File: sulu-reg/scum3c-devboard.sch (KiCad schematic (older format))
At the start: 36 parts, among them J1 Conn_02x11_Odd_Even, J2 Conn_02x10_Odd_Even, J3 Conn_02x05_Odd_Even, J4 73391-0060, U2 S-85S1AB18-I6T1U, U3 S-85S1AB11-I6T1U, U9AB1 ICM-20948

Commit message: finished routing
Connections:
- net +1.1V_REG: now also J1.8 (Pin_8); no longer J1.10 (Pin_10)
- net +1.8V_REG: now also J1.4 (Pin_4), J1.6 (Pin_6); no longer J1.14 (Pin_14), J1.16 (Pin_16)
- net +EXT_BAT: now also J1.12 (Pin_12), J1.9 (Pin_9); no longer J1.11 (Pin_11), J1.18 (Pin_18)
- net +VBAT: now also J1.17 (Pin_17), J1.5 (Pin_5); no longer J1.13 (Pin_13), J1.7 (Pin_7)
- net +VDDD: now also J1.7 (Pin_7); no longer J1.9 (Pin_9)
- net +VDDIO: now also J1.13 (Pin_13), J1.15 (Pin_15), J1.18 (Pin_18); no longer J1.3 (Pin_3), J1.5 (Pin_5), J1.8 (Pin_8)
- net 1.1V_IN: now also J1.10 (Pin_10); no longer J1.12 (Pin_12)
- net GND: now also J1.11 (Pin_11), J1.3 (Pin_3); no longer J1.15 (Pin_15), J1.17 (Pin_17)
- net IMU_VDD: now also J1.16 (Pin_16); no longer J1.6 (Pin_6)
- net IMU_VDDIO: now also J1.14 (Pin_14); no longer J1.4 (Pin_4)
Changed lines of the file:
@@
 Text Label 1700 1750 2    50   ~ 0
 IMU_VDDIO
-Text Label 1800 6900 0    50   ~ 0
+Text Label 1800 7400 0    50   ~ 0
 IMU_VDDIO
 Text Label 3800 7300 0    50   ~ 0
@@
 Text Label 3800 7600 0    50   ~ 0
 GPIO15
-Text Label 1800 7000 0    50   ~ 0
+Text Label 1800 7500 0    50   ~ 0
 IMU_VDD
 NoConn ~ 1300 2950
@@
 	0    1    1    0
 $EndComp
-Text Label 1800 7700 0    50   ~ 0
-BOOT_SOURCE_SEL
 Text Label 5450 7150 0    50   ~ 0
 3WB_DATA
@@
 	0    1    1    0
 $EndComp
-Text Label 1300 7800 2    50   ~ 0
-SENSOR_EXT_IN
-Text Label 1800 7800 0    50   ~ 0
-SENSOR_LDO_OUTPUT
 Text Label 4950 6950 2    50   ~ 0
 RsRx
@@
 L draft1library:+VDDIO #PWR?
 U 1 1 6076CC41
-P 1300 7000
+P 1300 7500
 AR Path="/5F3B1D81/6076CC41" Ref="#PWR?"  Part="1"
 AR Path="/6076CC41" Ref="#PWR05"  Part="1"
-F 0 "#PWR05" H 1300 6850 50  0001 C CNN
-F 1 "+VDDIO" V 1315 7128 50  0000 L CNN
-F 2 "" H 1300 7000 50  0001 C CNN
-F 3 "" H 1300 7000 50  0001 C CNN
-	1    1300 7000
+F 0 "#PWR05" H 1300 7350 50  0001 C CNN
+F 1 "+VDDIO" V 1315 7628 50  0000 L CNN
+F 2 "" H 1300 7500 50  0001 C CNN
+F 3 "" H 1300 7500 50  0001 C CNN
+	1    1300 7500
 	0    -1   -1   0
 $EndComp
@@
 L draft1library:+VDDIO #PWR?
 U 1 1 6076D2AC
-P 1300 6900
+P 1300 7400
 AR Path="/5F3B1D81/6076D2AC" Ref="#PWR?"  Part="1"
 AR Path="/6076D2AC" Ref="#PWR04"  Part="1"
-F 0 "#PWR04" H 1300 6750 50  0001 C CNN
-F 1 "+VDDIO" V 1315 7028 50  0000 L CNN
-F 2 "" H 1300 6900 50  0001 C CNN
-F 3 "" H 1300 6900 50  0001 C CNN
-	1    1300 6900
+F 0 "#PWR04" H 1300 7250 50  0001 C CNN
+F 1 "+VDDIO" V 1315 7528 50  0000 L CNN
+F 2 "" H 1300 7400 50  0001 C CNN
+F 3 "" H 1300 7400 50  0001 C CNN
+	1    1300 7400
 	0    -1   -1   0
 $EndComp
@@
 L draft1library:+VBAT #PWR?
 U 1 1 6076D7B9
-P 1300 7100
+P 1300 7600
 AR Path="/5F3B1D81/6076D7B9" Ref="#PWR?"  Part="1"
 AR Path="/5F41418C/6076D7B9" Ref="#PWR?"  Part="1"
 AR Path="/5F414989/6076D7B9" Ref="#PWR?"  Part="1"
 AR Path="/6076D7B9" Ref="#PWR06"  Part="1"
-F 0 "#PWR06" H 1300 6950 50  0001 C CNN
-F 1 "+VBAT" V 1300 7400 50  0000 C CNN
-F 2 "" H 1300 7100 50  0001 C CNN
-F 3 "" H 1300 7100 50  0001 C CNN
-	1    1300 7100
+F 0 "#PWR06" H 1300 7450 50  0001 C CNN
+F 1 "+VBAT" V 1300 7900 50  0000 C CNN
+F 2 "" H 1300 7600 50  0001 C CNN
+F 3 "" H 1300 7600 50  0001 C CNN
+	1    1300 7600
 	0    -1   -1   0
 $EndComp
@@
 L draft1library:+VBAT #PWR?
 U 1 1 6127ADAC
-P 1300 7400
+P 1300 7000
 AR Path="/5F3B1D81/6127ADAC" Ref="#PWR?"  Part="1"
 AR Path="/5F41418C/6127ADAC" Ref="#PWR?"  Part="1"
 AR Path="/5F414989/6127ADAC" Ref="#PWR?"  Part="1"
 AR Path="/6127ADAC" Ref="#PWR0107"  Part="1"
-F 0 "#PWR0107" H 1300 7250 50  0001 C CNN
-F 1 "+VBAT" V 1300 7700 50  0000 C CNN
-F 2 "" H 1300 7400 50  0001 C CNN
-F 3 "" H 1300 7400 50  0001 C CNN
-	1    1300 7400
+F 0 "#PWR0107" H 1300 6850 50  0001 C CNN
+F 1 "+VBAT" V 1300 7300 50  0000 C CNN
+F 2 "" H 1300 7000 50  0001 C CNN
+F 3 "" H 1300 7000 50  0001 C CNN
+	1    1300 7000
 	0    -1   -1   0
 $EndComp
@@
 L power:GND #PWR0108
 U 1 1 6127B18B
-P 1300 7500
-F 0 "#PWR0108" H 1300 7250 50  0001 C CNN
-F 1 "GND" V 1305 7372 50  0000 R CNN
-F 2 "" H 1300 7500 50  0001 C CNN
-F 3 "" H 1300 7500 50  0001 C CNN
-	1    1300 7500
-	0    1    1    0
-$EndComp
-$Comp
-L power:GND #PWR0109
-U 1 1 6127B4FF
-P 1300 7600
-F 0 "#PWR0109" H 1300 7350 50  0001 C CNN
-F 1 "GND" V 1305 7472 50  0000 R CNN
-F 2 "" H 1300 7600 50  0001 C CNN
-F 3 "" H 1300 7600 50  0001 C CNN
-	1    1300 7600
+P 1300 6900
+F 0 "#PWR0108" H 1300 6650 50  0001 C CNN
+F 1 "GND" V 1305 6772 50  0000 R CNN
+F 2 "" H 1300 6900 50  0001 C CNN
+F 3 "" H 1300 6900 50  0001 C CNN
+	1    1300 6900
 	0    1    1    0
 $EndComp
@@
 L draft1library:+1.1V_REG #PWR0110
 U 1 1 61280E78
-P 1800 7200
-F 0 "#PWR0110" H 1800 7050 50  0001 C CNN
-F 1 "+1.1V_REG" V 1815 7328 50  0000 L CNN
-F 2 "" H 1800 7200 50  0001 C CNN
-F 3 "" H 1800 7200 50  0001 C CNN
-	1    1800 7200
-	0    1    1    0
-$EndComp
-$Comp
-L draft1library:+1.8V_REG #PWR0111
-U 1 1 61281B91
-P 1800 7400
-F 0 "#PWR0111" H 1800 7250 50  0001 C CNN
-F 1 "+1.8V_REG" V 1815 7528 50  0000 L CNN
-F 2 "" H 1800 7400 50  0001 C CNN
-F 3 "" H 1800 7400 50  0001 C CNN
-	1    1800 7400
+P 1800 7100
+F 0 "#PWR0110" H 1800 6950 50  0001 C CNN
+F 1 "+1.1V_REG" V 1815 7228 50  0000 L CNN
+F 2 "" H 1800 7100 50  0001 C CNN
+F 3 "" H 1800 7100 50  0001 C CNN
+	1    1800 7100
 	0    1    1    0
 $EndComp
@@
 L draft1library:+1.8V_REG #PWR0112
 U 1 1 612829BE
-P 1800 7500
-F 0 "#PWR0112" H 1800 7350 50  0001 C CNN
-F 1 "+1.8V_REG" V 1815 7628 50  0000 L CNN
-F 2 "" H 1800 7500 50  0001 C CNN
-F 3 "" H 1800 7500 50  0001 C CNN
-	1    1800 7500
-	0    1    1    0
-$EndComp
-$Comp
-L draft1library:+EXT_BAT #PWR0113
-U 1 1 612835E6
-P 1800 7600
-F 0 "#PWR0113" H 1800 7450 50  0001 C CNN
-F 1 "+EXT_BAT" V 1815 7728 50  0000 L CNN
-F 2 "" H 1800 7600 50  0001 C CNN
-F 3 "" H 1800 7600 50  0001 C CNN
-	1    1800 7600
+P 1800 6900
+F 0 "#PWR0112" H 1800 6750 50  0001 C CNN
+F 1 "+1.8V_REG" V 1815 7028 50  0000 L CNN
+F 2 "" H 1800 6900 50  0001 C CNN
+F 3 "" H 1800 6900 50  0001 C CNN
+	1    1800 6900
 	0    1    1    0
 $EndComp
@@
 L draft1library:+VDDD #PWR0125
 U 1 1 612C7D86
-P 1300 7200
-F 0 "#PWR0125" H 1300 7050 50  0001 C CNN
-F 1 "+VDDD" V 1300 7500 50  0000 C CNN
-F 2 "" H 1300 7200 50  0001 C CNN
-F 3 "" H 1300 7200 50  0001 C CNN
-	1    1300 7200
+P 1300 7100
+F 0 "#PWR0125" H 1300 6950 50  0001 C CNN
+F 1 "+VDDD" V 1300 7400 50  0000 C CNN
+F 2 "" H 1300 7100 50  0001 C CNN
+F 3 "" H 1300 7100 50  0001 C CNN
+	1    1300 7100
 	0    -1   -1   0
 $EndComp
@@
 L draft1library:+VDDIO #PWR?
 U 1 1 6076E794
-P 1800 7100
+P 1800 7600
 AR Path="/5F3B1D81/6076E794" Ref="#PWR?"  Part="1"
 AR Path="/6076E794" Ref="#PWR08"  Part="1"
-F 0 "#PWR08" H 1800 6950 50  0001 C CNN
-F 1 "+VDDIO" V 1800 7250 50  0000 L CNN
-F 2 "" H 1800 7100 50  0001 C CNN
-F 3 "" H 1800 7100 50  0001 C CNN
-	1    1800 7100
-	0    1    1    0
-$EndComp
-$Comp
-L draft1library:+VDDD #PWR07
-U 1 1 60769F1D
-P 1300 7700
-F 0 "#PWR07" H 1300 7550 50  0001 C CNN
-F 1 "+VDDD" V 1300 8000 50  0000 C CNN
-F 2 "" H 1300 7700 50  0001 C CNN
-F 3 "" H 1300 7700 50  0001 C CNN
-	1    1300 7700
-	0    -1   -1   0
+F 0 "#PWR08" H 1800 7450 50  0001 C CNN
+F 1 "+VDDIO" V 1800 7750 50  0000 L CNN
+F 2 "" H 1800 7600 50  0001 C CNN
+F 3 "" H 1800 7600 50  0001 C CNN
+	1    1800 7600
+	0    1    1    0
 $EndComp
 $Comp
@@
 	1    0    0    -1
 $EndComp
-Text Label 1800 7300 0    50   ~ 0
-1.1V_IN
-$Comp
-L draft1library:+EXT_BAT #PWR0123
-U 1 1 6136676E
-P 1300 7300
-F 0 "#PWR0123" H 1300 7150 50  0001 C CNN
-F 1 "+EXT_BAT" V 1315 7428 50  0000 L CNN
-F 2 "" H 1300 7300 50  0001 C CNN
-F 3 "" H 1300 7300 50  0001 C CNN
-	1    1300 7300
-	0    -1   -1   0
-$EndComp
 Text Label 1200 5300 2    50   ~ 0
 1.1V_IN
@@
 	1    0    0    -1
 $EndComp
+$Comp
+L draft1library:+EXT_BAT #PWR0123
+U 1 1 6136676E
+P 1300 7200
+F 0 "#PWR0123" H 1300 7050 50  0001 C CNN
+F 1 "+EXT_BAT" V 1315 7328 50  0000 L CNN
+F 2 "" H 1300 7200 50  0001 C CNN
+F 3 "" H 1300 7200 50  0001 C CNN
+	1    1300 7200
+	0    -1   -1   0
+$EndComp
+Text Label 1800 7200 0    50   ~ 0
+1.1V_IN
+$Comp
+L draft1library:+VDDD #PWR07
+U 1 1 60769F1D
+P 1300 7700
+F 0 "#PWR07" H 1300 7550 50  0001 C CNN
+F 1 "+VDDD" V 1300 8000 50  0000 C CNN
+F 2 "" H 1300 7700 50  0001 C CNN
+F 3 "" H 1300 7700 50  0001 C CNN
+	1    1300 7700
+	0    -1   -1   0
+$EndComp
+$Comp
+L draft1library:+EXT_BAT #PWR0113
+U 1 1 612835E6
+P 1800 7300
+F 0 "#PWR0113" H 1800 7150 50  0001 C CNN
+F 1 "+EXT_BAT" V 1800 7450 50  0000 L CNN
+F 2 "" H 1800 7300 50  0001 C CNN
+F 3 "" H 1800 7300 50  0001 C CNN
+	1    1800 7300
+	0    1    1    0
+$EndComp
+$Comp
+L draft1library:+1.8V_REG #PWR0111
+U 1 1 61281B91
+P 1800 7000
+F 0 "#PWR0111" H 1800 6850 50  0001 C CNN
+F 1 "+1.8V_REG" V 1815 7128 50  0000 L CNN
+F 2 "" H 1800 7000 50  0001 C CNN
+F 3 "" H 1800 7000 50  0001 C CNN
+	1    1800 7000
+	0    1    1    0
+$EndComp
+$Comp
+L power:GND #PWR0109
+U 1 1 6127B4FF
+P 1300 7300
+F 0 "#PWR0109" H 1300 7050 50  0001 C CNN
+F 1 "GND" V 1305 7172 50  0000 R CNN
+F 2 "" H 1300 7300 50  0001 C CNN
+F 3 "" H 1300 7300 50  0001 C CNN
+	1    1300 7300
+	0    1    1    0
+$EndComp
+Text Label 1800 7800 0    50   ~ 0
+SENSOR_LDO_OUTPUT
+Text Label 1300 7800 2    50   ~ 0
+SENSOR_EXT_IN
+Text Label 1800 7700 0    50   ~ 0
+BOOT_SOURCE_SEL
 $EndSCHEMATC

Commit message: switched out dc-dc converter footprints to recommended components
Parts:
- C_1.1_OUT1, C_1.8_OUT1: footprint Capacitor_SMD:C_0805_2012Metric -> Capacitor_SMD:C_0402_1005Metric
- L1, L2: footprint Inductor_SMD:L_0402_1005Metric -> Inductor_SMD:L_Wuerth_MAPI-2010
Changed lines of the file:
@@
 F 0 "C_1.8_OUT1" H 3092 4496 50  0000 L CNN
 F 1 "100 uF" H 3092 4405 50  0000 L CNN
-F 2 "Capacitor_SMD:C_0805_2012Metric" H 3000 4450 50  0001 C CNN
+F 2 "Capacitor_SMD:C_0402_1005Metric" H 3000 4450 50  0001 C CNN
 F 3 "~" H 3000 4450 50  0001 C CNN
 	1    3000 4450
@@
 F 0 "L1" V 2650 4400 50  0000 L CNN
 F 1 "2.2 uH" V 2750 4350 50  0000 L CNN
-F 2 "Inductor_SMD:L_0402_1005Metric" H 2700 4450 50  0001 C CNN
+F 2 "Inductor_SMD:L_Wuerth_MAPI-2010" H 2700 4450 50  0001 C CNN
 F 3 "~" H 2700 4450 50  0001 C CNN
 	1    2700 4450
@@
 F 0 "C_1.1_OUT1" H 3500 5450 50  0000 R CNN
 F 1 "100 uF" H 3350 5350 50  0000 R CNN
-F 2 "Capacitor_SMD:C_0805_2012Metric" H 3000 5400 50  0001 C CNN
+F 2 "Capacitor_SMD:C_0402_1005Metric" H 3000 5400 50  0001 C CNN
 F 3 "~" H 3000 5400 50  0001 C CNN
 	1    3000 5400
@@
 F 0 "L2" V 2650 5350 50  0000 L CNN
 F 1 "2.2 uH" V 2750 5300 50  0000 L CNN
-F 2 "Inductor_SMD:L_0402_1005Metric" H 2700 5400 50  0001 C CNN
+F 2 "Inductor_SMD:L_Wuerth_MAPI-2010" H 2700 5400 50  0001 C CNN
 F 3 "~" H 2700 5400 50  0001 C CNN
 	1    2700 5400

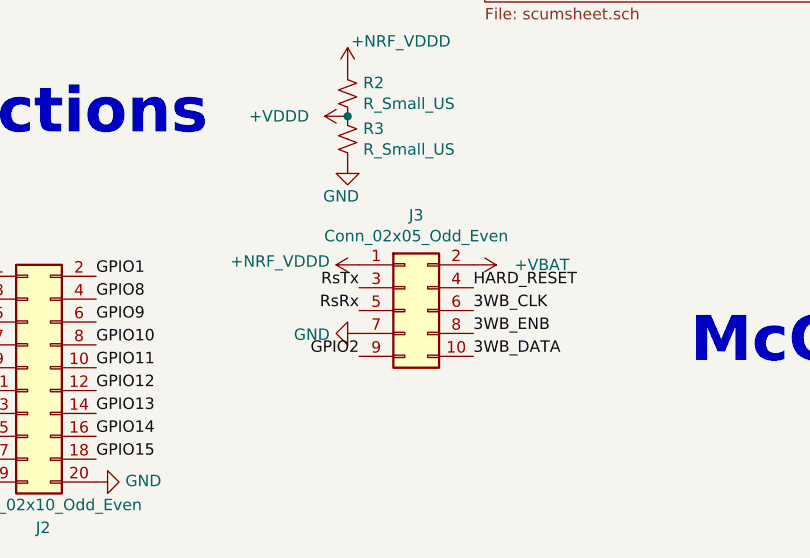
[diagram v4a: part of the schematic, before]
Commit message: changed 2x5 to 1x10 nrf header
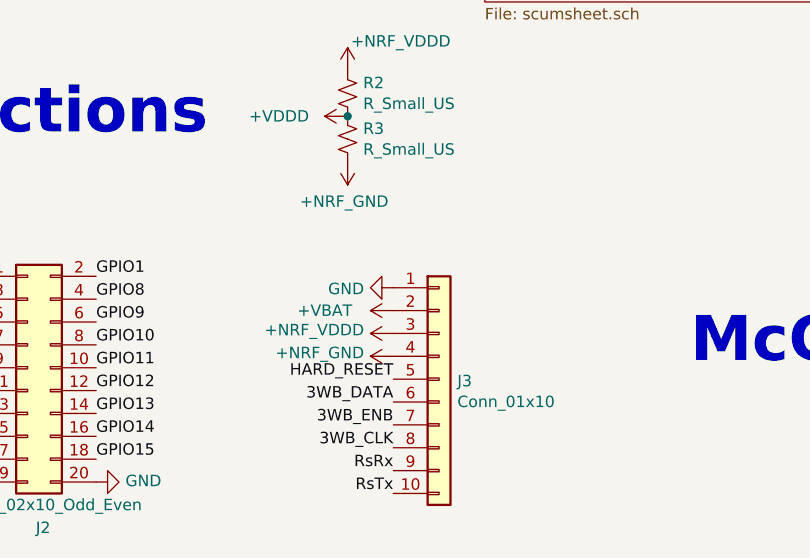
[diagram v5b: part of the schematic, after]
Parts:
- removed J3: Conn_02x05_Odd_Even, Connector_PinHeader_2.54mm:PinHeader_2x05_P2.54mm_Vertical, symbol Connector_Generic:Conn_02x05_Odd_Even
- added J3: Conn_01x10, Connector_PinHeader_2.54mm:PinHeader_1x10_P2.54mm_Vertical, symbol Connector_Generic:Conn_01x10
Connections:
- net +NRF_VDDD: now also J3.3 (Pin_3)
- net +VBAT: now also J3.2 (Pin_2)
- net 3WB_CLK: now also J3.8 (Pin_8)
- net 3WB_DATA: now also J3.6 (Pin_6)
- net 3WB_ENB: now also J3.7 (Pin_7)
- net GND: now also J3.1 (Pin_1); no longer R3.2
- net HARD_RESET: now also J3.5 (Pin_5)
- net RsRx: now also J3.9 (Pin_9)
- net RsTx: now also J3.10 (Pin_10)
- new net +NRF_GND: J3.4 (Pin_4), R3.2
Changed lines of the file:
@@
 L power:GND #PWR021
 U 1 1 607605CB
-P 4950 7050
-F 0 "#PWR021" H 4950 6800 50  0001 C CNN
-F 1 "GND" V 4955 6922 50  0000 R CNN
-F 2 "" H 4950 7050 50  0001 C CNN
-F 3 "" H 4950 7050 50  0001 C CNN
-	1    4950 7050
-	0    1    1    0
-$EndComp
-Text Label 5450 7150 0    50   ~ 0
+P 5100 6850
+F 0 "#PWR021" H 5100 6600 50  0001 C CNN
+F 1 "GND" V 5105 6722 50  0000 R CNN
+F 2 "" H 5100 6850 50  0001 C CNN
+F 3 "" H 5100 6850 50  0001 C CNN
+	1    5100 6850
+	0    1    1    0
+$EndComp
+Text Label 5100 7350 2    50   ~ 0
 3WB_DATA
-Text Label 5450 7050 0    50   ~ 0
+Text Label 5100 7450 2    50   ~ 0
 3WB_ENB
-Text Label 5450 6950 0    50   ~ 0
+Text Label 5100 7550 2    50   ~ 0
 3WB_CLK
-Text Label 5450 6850 0    50   ~ 0
+Text Label 5100 7250 2    50   ~ 0
 HARD_RESET
 $Comp
 L draft1library:+VBAT #PWR?
 U 1 1 60769236
-P 5450 6750
+P 5100 6950
 AR Path="/5F3B1D81/60769236" Ref="#PWR?"  Part="1"
 AR Path="/5F41418C/60769236" Ref="#PWR?"  Part="1"
 AR Path="/5F414989/60769236" Ref="#PWR?"  Part="1"
 AR Path="/60769236" Ref="#PWR024"  Part="1"
-F 0 "#PWR024" H 5450 6600 50  0001 C CNN
-F 1 "+VBAT" V 5450 7050 50  0000 C CNN
-F 2 "" H 5450 6750 50  0001 C CNN
-F 3 "" H 5450 6750 50  0001 C CNN
-	1    5450 6750
-	0    1    1    0
-$EndComp
-Text Label 4950 6950 2    50   ~ 0
+F 0 "#PWR024" H 5100 6800 50  0001 C CNN
+F 1 "+VBAT" V 5100 7250 50  0000 C CNN
+F 2 "" H 5100 6950 50  0001 C CNN
+F 3 "" H 5100 6950 50  0001 C CNN
+	1    5100 6950
+	0    -1   -1   0
+$EndComp
+Text Label 5100 7650 2    50   ~ 0
 RsRx
-Text Label 4950 6850 2    50   ~ 0
+Text Label 5100 7750 2    50   ~ 0
 RsTx
 $Comp
@@
 	0    -1   -1   0
 $EndComp
-Text Label 4950 7150 2    50   ~ 0
-GPIO2
 $Comp
 L draft1library:+VBAT #PWR?
@@
 $EndComp
 $Comp
-L Connector_Generic:Conn_02x05_Odd_Even J3
-U 1 1 61289652
-P 5150 6950
-F 0 "J3" H 5200 7367 50  0000 C CNN
-F 1 "Conn_02x05_Odd_Even" H 5200 7276 50  0000 C CNN
-F 2 "Connector_PinHeader_2.54mm:PinHeader_2x05_P2.54mm_Vertical" H 5150 6950 50  0001 C CNN
-F 3 "~" H 5150 6950 50  0001 C CNN
-	1    5150 6950
-	1    0    0    -1
-$EndComp
-$Comp
 L draft1library:+NRF_VDDD #PWR0114
 U 1 1 61280205
-P 4950 6750
-F 0 "#PWR0114" H 4950 6600 50  0001 C CNN
-F 1 "+NRF_VDDD" V 4965 6878 50  0000 L CNN
-F 2 "" H 4950 6750 50  0001 C CNN
-F 3 "" H 4950 6750 50  0001 C CNN
-	1    4950 6750
+P 5100 7050
+F 0 "#PWR0114" H 5100 6900 50  0001 C CNN
+F 1 "+NRF_VDDD" V 5115 7178 50  0000 L CNN
+F 2 "" H 5100 7050 50  0001 C CNN
+F 3 "" H 5100 7050 50  0001 C CNN
+	1    5100 7050
 	0    -1   -1   0
 $EndComp
@@
 F 3 "" H 4900 5900 50  0001 C CNN
 	1    4900 5900
-	1    0    0    -1
-$EndComp
-$Comp
-L power:GND #PWR0128
-U 1 1 6137B87E
-P 4900 6300
-F 0 "#PWR0128" H 4900 6050 50  0001 C CNN
-F 1 "GND" H 4950 6150 50  0000 R CNN
-F 2 "" H 4900 6300 50  0001 C CNN
-F 3 "" H 4900 6300 50  0001 C CNN
-	1    4900 6300
 	1    0    0    -1
 $EndComp
@@
 Text Label 1800 7700 0    50   ~ 0
 BOOT_SOURCE_SEL
+$Comp
+L draft1library:+NRF_GND #PWR0128
+U 1 1 619A2365
+P 5100 7150
+F 0 "#PWR0128" H 5100 7000 50  0001 C CNN
+F 1 "+NRF_GND" V 5115 7278 50  0000 L CNN
+F 2 "" H 5100 7150 50  0001 C CNN
+F 3 "" H 5100 7150 50  0001 C CNN
+	1    5100 7150
+	0    -1   -1   0
+$EndComp
+$Comp
+L draft1library:+NRF_GND #PWR0130
+U 1 1 619A311C
+P 4900 6300
+F 0 "#PWR0130" H 4900 6150 50  0001 C CNN
+F 1 "+NRF_GND" H 4915 6473 50  0000 C CNN
+F 2 "" H 4900 6300 50  0001 C CNN
+F 3 "" H 4900 6300 50  0001 C CNN
+	1    4900 6300
+	-1   0    0    1
+$EndComp
+$Comp
+L Connector_Generic:Conn_01x10 J3
+U 1 1 619A3CA9
+P 5300 7250
+F 0 "J3" H 5380 7242 50  0000 L CNN
+F 1 "Conn_01x10" H 5380 7151 50  0000 L CNN
+F 2 "Connector_PinHeader_2.54mm:PinHeader_1x10_P2.54mm_Vertical" H 5300 7250 50  0001 C CNN
+F 3 "~" H 5300 7250 50  0001 C CNN
+	1    5300 7250
+	1    0    0    -1
+$EndComp
 $EndSCHEMATC

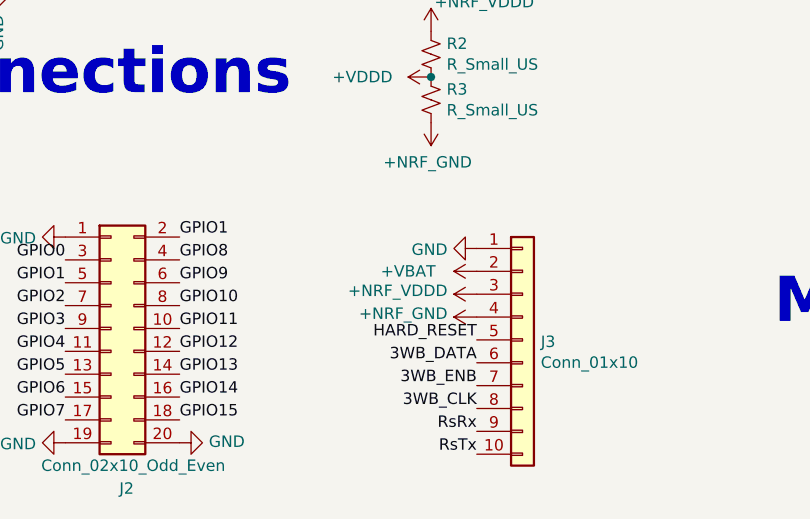
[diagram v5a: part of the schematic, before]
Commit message: brought images up to date with single row nrf
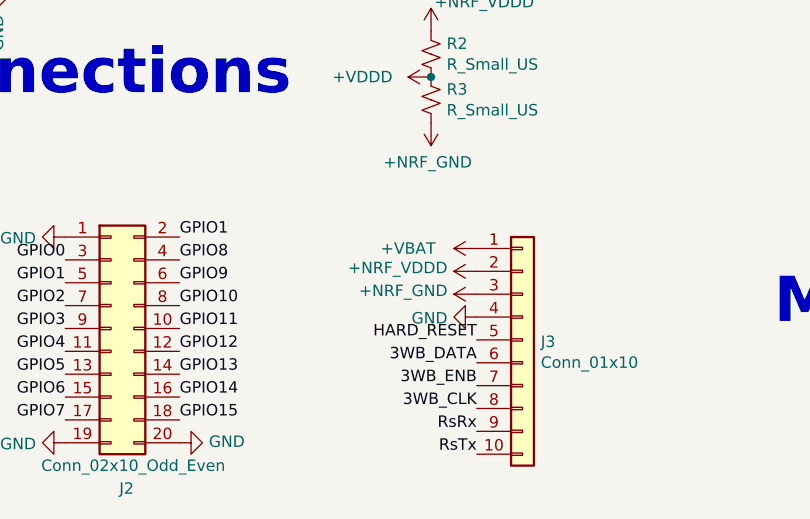
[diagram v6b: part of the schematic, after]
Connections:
- net +NRF_GND: now also J3.3 (Pin_3); no longer J3.4 (Pin_4)
- net +NRF_VDDD: now also J3.2 (Pin_2); no longer J3.3 (Pin_3)
- net +VBAT: now also J3.1 (Pin_1); no longer J3.2 (Pin_2)
- net GND: now also J3.4 (Pin_4); no longer J3.1 (Pin_1)
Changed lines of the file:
@@
 L power:GND #PWR021
 U 1 1 607605CB
-P 5100 6850
-F 0 "#PWR021" H 5100 6600 50  0001 C CNN
-F 1 "GND" V 5105 6722 50  0000 R CNN
-F 2 "" H 5100 6850 50  0001 C CNN
-F 3 "" H 5100 6850 50  0001 C CNN
-	1    5100 6850
+P 5100 7150
+F 0 "#PWR021" H 5100 6900 50  0001 C CNN
+F 1 "GND" V 5105 7022 50  0000 R CNN
+F 2 "" H 5100 7150 50  0001 C CNN
+F 3 "" H 5100 7150 50  0001 C CNN
+	1    5100 7150
 	0    1    1    0
 $EndComp
@@
 L draft1library:+VBAT #PWR?
 U 1 1 60769236
-P 5100 6950
+P 5100 6850
 AR Path="/5F3B1D81/60769236" Ref="#PWR?"  Part="1"
 AR Path="/5F41418C/60769236" Ref="#PWR?"  Part="1"
 AR Path="/5F414989/60769236" Ref="#PWR?"  Part="1"
 AR Path="/60769236" Ref="#PWR024"  Part="1"
-F 0 "#PWR024" H 5100 6800 50  0001 C CNN
-F 1 "+VBAT" V 5100 7250 50  0000 C CNN
-F 2 "" H 5100 6950 50  0001 C CNN
-F 3 "" H 5100 6950 50  0001 C CNN
-	1    5100 6950
+F 0 "#PWR024" H 5100 6700 50  0001 C CNN
+F 1 "+VBAT" V 5100 7150 50  0000 C CNN
+F 2 "" H 5100 6850 50  0001 C CNN
+F 3 "" H 5100 6850 50  0001 C CNN
+	1    5100 6850
 	0    -1   -1   0
 $EndComp
@@
 L draft1library:+NRF_VDDD #PWR0114
 U 1 1 61280205
-P 5100 7050
-F 0 "#PWR0114" H 5100 6900 50  0001 C CNN
-F 1 "+NRF_VDDD" V 5115 7178 50  0000 L CNN
-F 2 "" H 5100 7050 50  0001 C CNN
-F 3 "" H 5100 7050 50  0001 C CNN
-	1    5100 7050
+P 5100 6950
+F 0 "#PWR0114" H 5100 6800 50  0001 C CNN
+F 1 "+NRF_VDDD" V 5115 7078 50  0000 L CNN
+F 2 "" H 5100 6950 50  0001 C CNN
+F 3 "" H 5100 6950 50  0001 C CNN
+	1    5100 6950
 	0    -1   -1   0
 $EndComp
@@
 L draft1library:+NRF_GND #PWR0128
 U 1 1 619A2365
-P 5100 7150
-F 0 "#PWR0128" H 5100 7000 50  0001 C CNN
-F 1 "+NRF_GND" V 5115 7278 50  0000 L CNN
-F 2 "" H 5100 7150 50  0001 C CNN
-F 3 "" H 5100 7150 50  0001 C CNN
-	1    5100 7150
-	0    -1   -1   0
-$EndComp
+P 5100 7050
+F 0 "#PWR0128" H 5100 6900 50  0001 C CNN
+F 1 "+NRF_GND" V 5115 7178 50  0000 L CNN
+F 2 "" H 5100 7050 50  0001 C CNN
+F 3 "" H 5100 7050 50  0001 C CNN
+	1    5100 7050
+	0    -1   -1   0
+$EndComp
